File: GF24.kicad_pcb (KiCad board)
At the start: 2 copper layers, 110 x 40 mm, 65 parts, among them J1 3220-10-0300-00, Q1 3904, Q2 DMN3731U-7, Q3 DMN3731U-7, Q4 DMP2004K-7, Q5 DMP2004K-7, Q6 DMP2004K-7, SW1 NRST, SW2 BOOT, SW3 ACTION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

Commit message: going to try and reroute everything
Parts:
- removed BAT1, BAT2: Conn_01x01_Pin, MB-Battery:54
- removed BZ1: CSQG703BP, MB-Buzzer:CSQG703BP
- removed C1, C11, C2: 4.7uF, MB-Generic:C1206_medium
- removed C10, C13, C15, C8, C9: 1uF, MB-Generic:C0805_medium
- removed C12, C14, C4: 0.1uF, MB-Generic:C0603_medium
- removed C3: 10nF, MB-Generic:C0402_medium
- removed C5, C6: 10pF, MB-Generic:C0402_medium
- removed D1: D, MB-SOD:SOD-123-2
- removed D2, D3, D4: LED, MB-Opto:Kingbright-APDA3020
- removed D5: APBDA3020SURKCGKC-GX, MB-Opto:Kingbright-APBDA3020
- removed J1: 3220-10-0300-00, MB-Conn:CONN_3220-10-0100-00_CNC
- removed Q1: 3904, MB-SOT:SOT-23-3
- removed Q2, Q3: DMN3731U-7, MB-SOT:SOT-23-3
- removed Q4, Q5, Q6: DMP2004K-7, MB-SOT:SOT-23-3
- removed R1, R10, R13, R19, R21, R4: 10k, MB-Generic:R0603_medium
- removed R11, R12: 4.7k, MB-Generic:R0603_medium
- removed R14, R17, R18, R20, R22, R23, R3: 1k, MB-Generic:R0603_medium
- removed R15, R16: 47, MB-Generic:R0603_medium
- removed R2: 180, MB-Generic:R0603_medium
- removed R5: 1.5k, MB-Generic:R0603_medium
- removed R6: 4.12k, MB-Generic:R0603_medium
- removed R7, R8: 127, MB-Generic:R0603_medium
- removed R9: 51, MB-Generic:R0603_medium
- removed SW1: NRST, MB-SW:PTS815SJM250SMTRLFS
- removed SW2: BOOT, MB-SW:CJS-1200TA
- removed SW3: ACTION, Connector_Molex:Molex_MicroClasp_55932-0410_1x04_P2.00mm_Vertical
- removed SW4: ON/OFF, MB-SW:1101M2S5AQE2
- removed SW5: MODE, MB-SW:1101M2S5AQE2
- removed TH1: 10K, MB-Generic:R0603_medium
- removed U1: STM32F031C4T6, MB-STM:LQFP-48_7x7mm_P0.5mm
- removed U2: SAM-M10Q, MB-GNSS:SAM-M10Q
- removed U3: TPS745, MB-DFN:6-WDFN
- removed U4: LTC1733, MB-MSOP:10-MSOP
- removed U5: M24256, MB-DFN:8-UFDFN
- removed U6: 2137160001, MB-Conn:MOLEX_2137160001
- removed Y1: CS06465-32M, MB-Crystal:CS06465-32M
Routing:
- net GND: track 71.2 -> 0.00 mm, vias 34 -> 0
- net PG: track 65.5 -> 0.00 mm, vias 1 -> 0
- net N-CHRG: track 55.0 -> 0.00 mm
- net GNSS-TIMEPULSE: track 50.9 -> 0.00 mm
- net NRST: track 45.5 -> 0.00 mm
- net GNSS-N-RESET: track 44.2 -> 0.00 mm
- net MODE: track 41.0 -> 0.00 mm
- net N-FAULT: track 36.2 -> 0.00 mm
- net 3V3: track 35.7 -> 0.00 mm, vias 3 -> 0
- net BUTTON: track 33.9 -> 0.00 mm
- net STM32-TX: track 33.7 -> 0.00 mm
- net STM32-RX: track 33.4 -> 0.00 mm
- net /MODE-H: track 32.0 -> 0.00 mm
- net STATR: track 18.8 -> 0.00 mm, vias 1 -> 0
- net SDA: track 18.3 -> 0.00 mm
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- removed copper zone on F.Cu, net /REG_I
- removed copper zone on F.Cu, net 3V3
- removed copper zone on F.Cu, net BAT+
- removed copper zone on B.Cu, net GND
- removed copper zone on F.Cu, net VBUS
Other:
- board outline removed

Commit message: making things smaller
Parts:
- added C1: 4.7uF, MB-Generic:C1206_medium, F.Cu at (126.6, 62.2)
- added C10: 1uF, MB-Generic:C0805_medium, F.Cu at (168.0, 31.1)
- added C11: 4.7uF, MB-Generic:C1206_medium, F.Cu at (126.6, 68.9)
- added C12: 0.1uF, MB-Generic:C0603_medium, F.Cu at (134.9, 54.8)
- added C13: 1uF, MB-Generic:C0805_medium, F.Cu at (168.0, 34.2)
- added C14: 0.1uF, MB-Generic:C0603_medium, F.Cu at (134.9, 57.4)
- added C15: 1uF, MB-Generic:C0805_medium, F.Cu at (168.0, 37.2)
- added C2: 4.7uF, MB-Generic:C1206_medium, F.Cu at (126.6, 65.5)
- added C3: 10nF, MB-Generic:C0402_medium, F.Cu at (165.5, 67.0)
- added C4: 0.1uF, MB-Generic:C0603_medium, F.Cu at (134.9, 52.2)
- added C5: 10pF, MB-Generic:C0402_medium, F.Cu at (165.5, 69.1)
- added C6: 10pF, MB-Generic:C0402_medium, F.Cu at (165.5, 71.3)
- added C8: 1uF, MB-Generic:C0805_medium, F.Cu at (168.0, 25.1)
- added C9: 1uF, MB-Generic:C0805_medium, F.Cu at (168.0, 28.1)
- added CR1: M24C02-WMN6TP, MB-SOIC:SO-8_STM, F.Cu at (133.8, 63.8)
- added D1: D, MB-SOD:SOD-123-2, F.Cu at (161.3, 53.2)
- added D2: LED, MB-Opto:Kingbright-APDA3020, F.Cu at (146.9, 65.9)
- added D3: LED, MB-Opto:Kingbright-APDA3020, F.Cu at (146.9, 68.4)
- added D4: LED, MB-Opto:Kingbright-APDA3020, F.Cu at (146.9, 70.8)
- added D5: APBDA3020SURKCGKC-GX, MB-Opto:Kingbright-APBDA3020, F.Cu at (153.2, 70.7)
- added J1: Conn_ARM_SWD_TagConnect_TC2030, Connector:Tag-Connect_TC2030-IDC-FP_2x03_P1.27mm_Vertical, F.Cu at (128.5, 55.7)
- added J2: USB4110GFA, MB-Conn:GCT_USB4110GFA, F.Cu at (150.3, 57.8)
- added J3: S2B-PH-SM4-TB, MB-Conn:JST_S2B-PH-SM4-TB, F.Cu at (160.6, 32.1)
- added Q1: 3904, MB-SOT:SOT-23-3, F.Cu at (140.8, 42.8)
- added Q2: DMN3731U-7, MB-SOT:SOT-23-3, F.Cu at (140.8, 47.0)
- added Q3: DMN3731U-7, MB-SOT:SOT-23-3, F.Cu at (140.8, 51.2)
- added Q4: DMP2004K-7, MB-SOT:SOT-23-3, F.Cu at (140.8, 55.5)
- added Q5: DMP2004K-7, MB-SOT:SOT-23-3, F.Cu at (140.8, 59.7)
- added Q6: DMP2004K-7, MB-SOT:SOT-23-3, F.Cu at (140.8, 63.9)
- added R1: 10k, MB-Generic:R0603_medium, F.Cu at (145.2, 41.7)
- added R10: 10k, MB-Generic:R0603_medium, F.Cu at (148.9, 48.8)
- added R11: 4.7k, MB-Generic:R0603_medium, F.Cu at (148.9, 51.2)
- added R12: 4.7k, MB-Generic:R0603_medium, F.Cu at (148.9, 53.5)
- added R13: 10k, MB-Generic:R0603_medium, F.Cu at (152.6, 41.7)
- added R14: 1k, MB-Generic:R0603_medium, F.Cu at (152.6, 44.0)
- added R15: 47, MB-Generic:R0603_medium, F.Cu at (152.6, 46.4)
- added R16: 47, MB-Generic:R0603_medium, F.Cu at (152.6, 48.8)
- added R17: 1k, MB-Generic:R0603_medium, F.Cu at (152.6, 51.2)
- added R18: 1k, MB-Generic:R0603_medium, F.Cu at (152.6, 53.5)
- added R19: 10k, MB-Generic:R0603_medium, F.Cu at (156.3, 41.7)
- added R2: 180, MB-Generic:R0603_medium, F.Cu at (145.2, 44.0)
- added R20: 1k, MB-Generic:R0603_medium, F.Cu at (156.3, 44.0)
- added R21: 10k, MB-Generic:R0603_medium, F.Cu at (156.3, 46.4)
- added R22: 1k, MB-Generic:R0603_medium, F.Cu at (156.3, 48.8)
- added R23: 1k, MB-Generic:R0603_medium, F.Cu at (156.3, 51.2)
- added R3: 1k, MB-Generic:R0603_medium, F.Cu at (145.2, 46.4)
- added R4: 10k, MB-Generic:R0603_medium, F.Cu at (145.2, 48.8)
- added R5: 1.5k, MB-Generic:R0603_medium, F.Cu at (145.2, 51.2)
- added R6: 4.12k, MB-Generic:R0603_medium, F.Cu at (145.2, 53.5)
- added R7: 127, MB-Generic:R0603_medium, F.Cu at (148.9, 41.7)
- added R8: 127, MB-Generic:R0603_medium, F.Cu at (148.9, 44.0)
- added R9: 51, MB-Generic:R0603_medium, F.Cu at (148.9, 46.4)
- added SW1: ~, MB-SW:PTS815SJM250SMTRLFS, F.Cu at (160.7, 68.0)
- added SW2: BOOT, MB-SW:CJS-1200TA, F.Cu at (158.5, 37.5)
- added SW3: ~, MB-SW:TL1016AAF160QG, F.Cu at (153.6, 67.5)
- added SW4: ~, MB-SW:SW_500ASSP1SM6QE, F.Cu at (131.0, 30.5)
- added SW5: ~, MB-SW:SW_500ASSP1SM6QE, F.Cu at (131.0, 44.2)
- added TH1: 10K, MB-Generic:R0603_medium, F.Cu at (156.3, 53.5)
- added U1: STM32F031C4T6, MB-STM:LQFP-48_7x7mm_P0.5mm, F.Cu at (163.8, 46.2)
- added U2: SAM-M10Q, MB-GNSS:SAM-M10Q, F.Cu at (147.1, 32.0)
- added U3: TPS745, MB-DFN:6-WDFN, F.Cu at (169.3, 70.6)
- added U4: LTC1733, MB-MSOP:10-MSOP-TE, F.Cu at (133.0, 69.4)
- added U5: ST-025BH, MB-Buzzer:ST-025BH_SOB, F.Cu at (163.5, 60.4)
- added Y1: CS06465-32M, MB-Crystal:CS06465-32M, F.Cu at (169.2, 67.5)
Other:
- board outline added: 90 x 40 mm

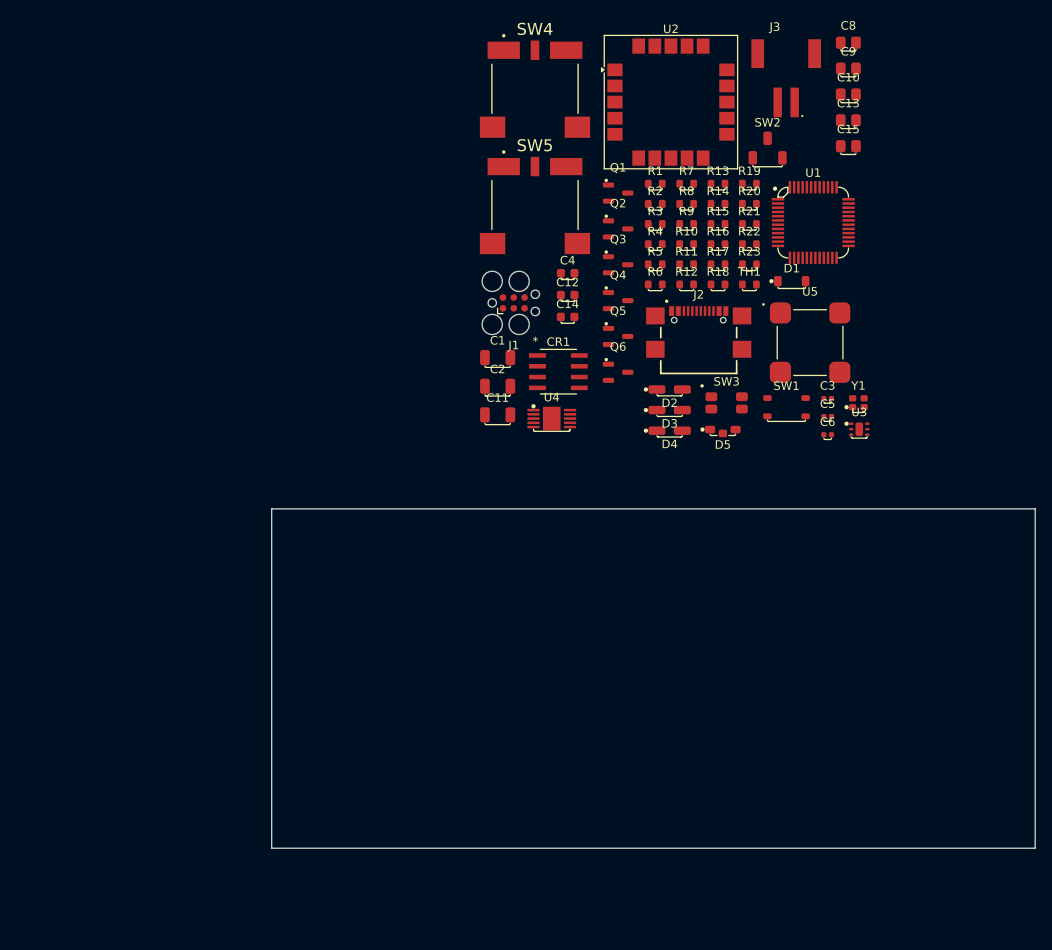
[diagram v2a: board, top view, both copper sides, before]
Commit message: added mouse bites. need to do stackup
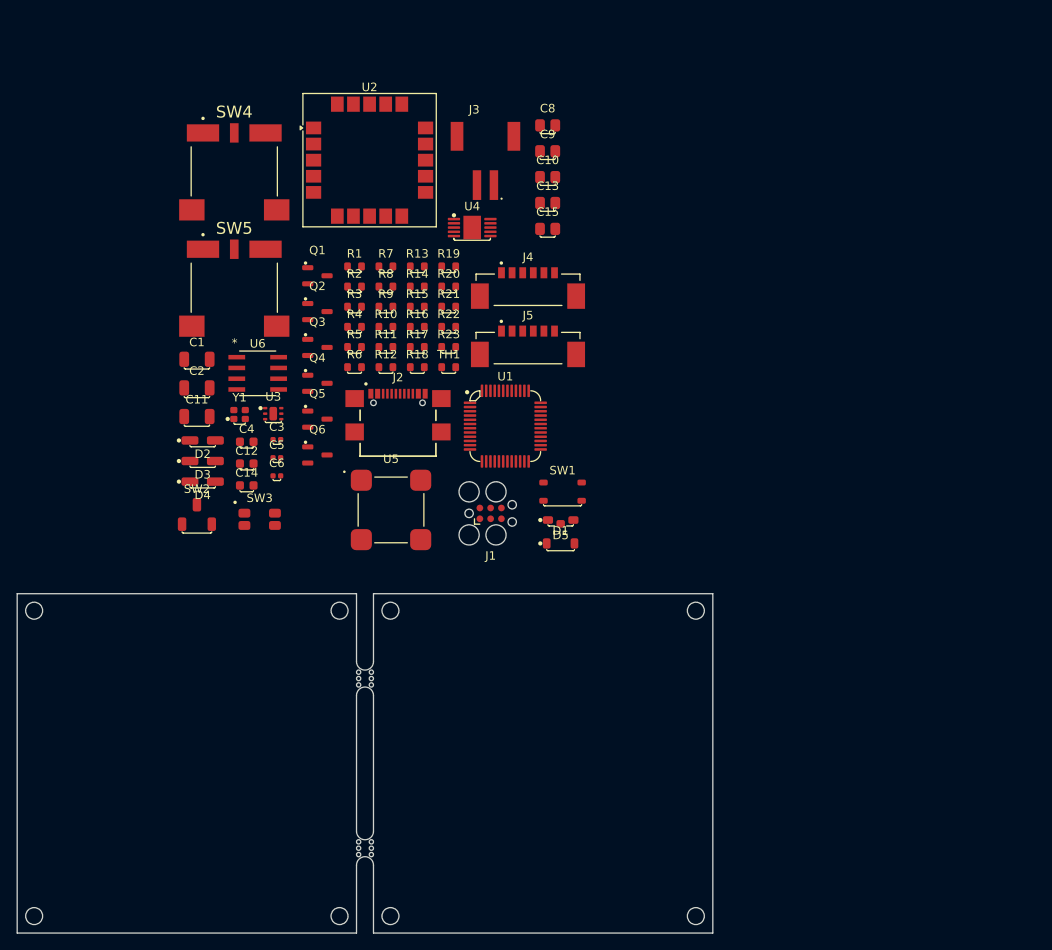
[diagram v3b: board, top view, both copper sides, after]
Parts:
- removed CR1: M24C02-WMN6TP, MB-SOIC:SO-8_STM
- added J4: 0533980671, MB-Conn:MOLEX_0533980671, F.Cu at (130.2, 52.8)
- added J5: 0533980671, MB-Conn:MOLEX_0533980671, F.Cu at (130.2, 59.7)
- added U6: M24C02-WMN6TP, MB-SOIC:SO-8_STM, F.Cu at (98.3, 64.0)
- added mouse-bite-2mm-slot: VAL**, MB-Tab:mouse-bite-2mm-slot, F.Cu at (111.0, 100.0)
- added mouse-bite-2mm-slot: VAL**, MB-Tab:mouse-bite-2mm-slot, F.Cu at (111.0, 120.0)
- J1: footprint Connector:Tag-Connect_TC2030-IDC-FP_2x03_P1.27mm_Vertical -> MB-Conn:Tag-Connect_TC2030-IDC-FP_2x03_P1.27mm_Vertical
- moved SW2 79.9 mm to (91.2, 80.7)
- moved Y1 73.0 mm to (96.2, 68.9)
- moved U3 69.1 mm to (100.2, 68.8)
- moved C3 65.1 mm to (100.6, 71.8)
- moved C5 65.1 mm to (100.6, 74.0)
- moved C6 65.1 mm to (100.6, 76.1)
- moved SW3 56.7 mm to (98.6, 81.2)
- moved D2 55.4 mm to (91.9, 71.9)
- moved D3 55.4 mm to (91.9, 74.4)
- moved D4 55.4 mm to (91.9, 76.8)
- moved U5 53.2 mm to (114.1, 80.1)
- moved U1 43.5 mm to (127.5, 70.2)
- moved C12 42.7 mm to (97.1, 74.7)
- moved C14 42.7 mm to (97.1, 77.2)
- moved C4 42.7 mm to (97.1, 72.1)
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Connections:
- U1 pad 11: GNSS-N-RESET -> /GNSS-ST-N-RESET
- U1 pad 12: GNSS-RX -> /GNSS-ST-RX
- U1 pad 13: GNSS-TX -> /GNSS-ST-TX
- U1 pad 14: GNSS-TIMEPULSE -> /GNSS-ST-TIMEPULSE
- U1 pad 42: unconnected-(U1-PB6-Pad42) -> BUZZER
- U2 pad 1: GND -> GNSS-GND
- U2 pad 10: GND -> GNSS-GND
- U2 pad 11: GND -> GNSS-GND
- U2 pad 15: GND -> GNSS-GND
- U2 pad 16: GND -> GNSS-GND
- U2 pad 17: +3V3 -> GNSS-3V3
- U2 pad 2: +3V3 -> GNSS-3V3
- U2 pad 20: GND -> GNSS-GND
- U2 pad 4: GND -> GNSS-GND
- U2 pad 5: GND -> GNSS-GND
- U2 pad 6: GND -> GNSS-GND
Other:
- board size 90 x 40 mm -> 82 x 40 mm

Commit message: board setup mostly complete. need to do net classes properly
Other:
- copper layers 2 -> 4
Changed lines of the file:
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@@
 	(generator_version "8.0")
 	(general
-		(thickness 1.6)
+		(thickness 1.547)
 		(legacy_teardrops no)
 	)
@@
 	(layers
 		(0 "F.Cu" signal)
+		(1 "In1.Cu" signal)
+		(2 "In2.Cu" signal)
 		(31 "B.Cu" signal)
 		(32 "B.Adhes" user "B.Adhesive")
@@
 			(layer "F.Cu"
 				(type "copper")
+				(thickness 0.0175)
+			)
+			(layer "dielectric 1"
+				(type "prepreg")
+				(thickness 0.196)
+				(material "7628")
+				(epsilon_r 4.74)
+				(loss_tangent 0.02)
+			)
+			(layer "In1.Cu"
+				(type "copper")
 				(thickness 0.035)
 			)
-			(layer "dielectric 1"
+			(layer "dielectric 2"
 				(type "core")
-				(thickness 1.51)
-				(material "FR4")
-				(epsilon_r 4.5)
+				(thickness 1.03)
+				(material "Core")
+				(epsilon_r 4.6)
+				(loss_tangent 0.02)
+			)
+			(layer "In2.Cu"
+				(type "copper")
+				(thickness 0.035)
+			)
+			(layer "dielectric 3"
+				(type "prepreg")
+				(thickness 0.196)
+				(material "7628")
+				(epsilon_r 4.74)
 				(loss_tangent 0.02)
 			)
 			(layer "B.Cu"
 				(type "copper")
-				(thickness 0.035)
+				(thickness 0.0175)
 			)
 			(layer "B.Mask"

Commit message: initial layout
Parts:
- C11, C12, C13, C15, D1, J1, J2, J3, J5, Q1, R13, R14, R2, R5, R6, SW4, SW5, TH1, U4, U5: moved to B.Cu
- moved Q1 79.5 mm to (130.2, 128.0), turned to 180 degrees
- moved J5 75.4 mm to (74.0, 110.0), turned to 90 degrees
- moved J4 75.3 mm to (124.0, 127.8), turned to 180 degrees
- moved U2 74.3 mm to (90.0, 110.0)
- moved U6 73.0 mm to (137.0, 126.0), turned to 90 degrees
- moved R2 73.0 mm to (130.5, 123.8), turned to 90 degrees
- moved C2 69.6 mm to (136.0, 119.0), turned to -135 degrees
- moved J3 69.5 mm to (120.0, 111.1), turned to -90 degrees
- moved C9 67.6 mm to (137.5, 105.2)
- moved C8 67.5 mm to (135.2, 102.2), turned to -90 degrees
- moved R11 65.1 mm to (138.0, 121.2)
- moved C13 62.6 mm to (124.5, 106.0), turned to -90 degrees
- moved SW4 62.2 mm to (123.0, 96.0)
- moved C15 62.0 mm to (138.2, 108.8)
- moved R12 62.0 mm to (139.0, 119.8)
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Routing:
- added copper zone on B.Cu, net GND
- added copper zone on F.Cu, net GND

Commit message: another round of layout
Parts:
- removed mouse-bite-2mm-slot (x2): VAL**, MB-Tab:mouse-bite-2mm-slot
- moved TH1 8.70 mm to (133.0, 110.2), turned to -90 degrees
- moved C12 2.80 mm to (135.8, 107.8)
- moved R7 2.49 mm to (141.5, 94.8), turned to 90 degrees
- moved R6 1.95 mm to (127.0, 108.0), turned to 180 degrees
- moved C11 1.35 mm to (133.8, 106.0)
- moved C15 1.27 mm to (139.5, 108.5)
- moved SW4 0.50 mm to (123.0, 96.5)
- moved SW5 0.50 mm to (141.0, 96.5)
- moved C2 0.32 mm to (136.2, 118.8)
- moved R3 0.15 mm to (150.3, 102.2)
- moved R4 0.15 mm to (147.3, 102.2)
- moved SW3 0.15 mm to (150.3, 98.2)
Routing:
- net GND: track 0.00 -> 74.9 mm, vias 0 -> 18
- net NRST: track 0.00 -> 48.6 mm, vias 0 -> 3
- net GNSS-GND: track 0.00 -> 34.2 mm, vias 0 -> 62
- net GNSS-TX: track 0.00 -> 25.5 mm, vias 0 -> 2
- net GNSS-RX: track 0.00 -> 25.4 mm, vias 0 -> 2
- net /SWDCLK: track 0.00 -> 22.4 mm, vias 0 -> 2
- net N-CHRG: track 0.00 -> 22.2 mm, vias 0 -> 2
- net STATR: track 0.00 -> 22.0 mm, vias 0 -> 2
- net BUTTON: track 0.00 -> 21.3 mm, vias 0 -> 2
- net +3V3: track 0.00 -> 21.1 mm, vias 0 -> 3
- net GNSS-N-RESET: track 0.00 -> 20.9 mm, vias 0 -> 2
- net /SWDIO: track 0.00 -> 20.7 mm, vias 0 -> 2
- net VBUS: track 0.00 -> 19.4 mm, vias 0 -> 4
- net GNSS-TIMEPULSE: track 0.00 -> 18.0 mm, vias 0 -> 2
- net MODE: track 0.00 -> 16.6 mm, vias 0 -> 3
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- added copper zone on F.Cu, net +3V3
- added copper zone on In2.Cu, net /REG_I
- added copper zone on B.Cu, net BAT+
- added copper zone on In1.Cu, net GNSS-3V3
- added copper zone on B.Cu, net GNSS-GND
- added copper zone on F.Cu, net GNSS-GND
- added copper zone on B.Cu, net VBUS
- removed copper zone on F.Cu, net GND

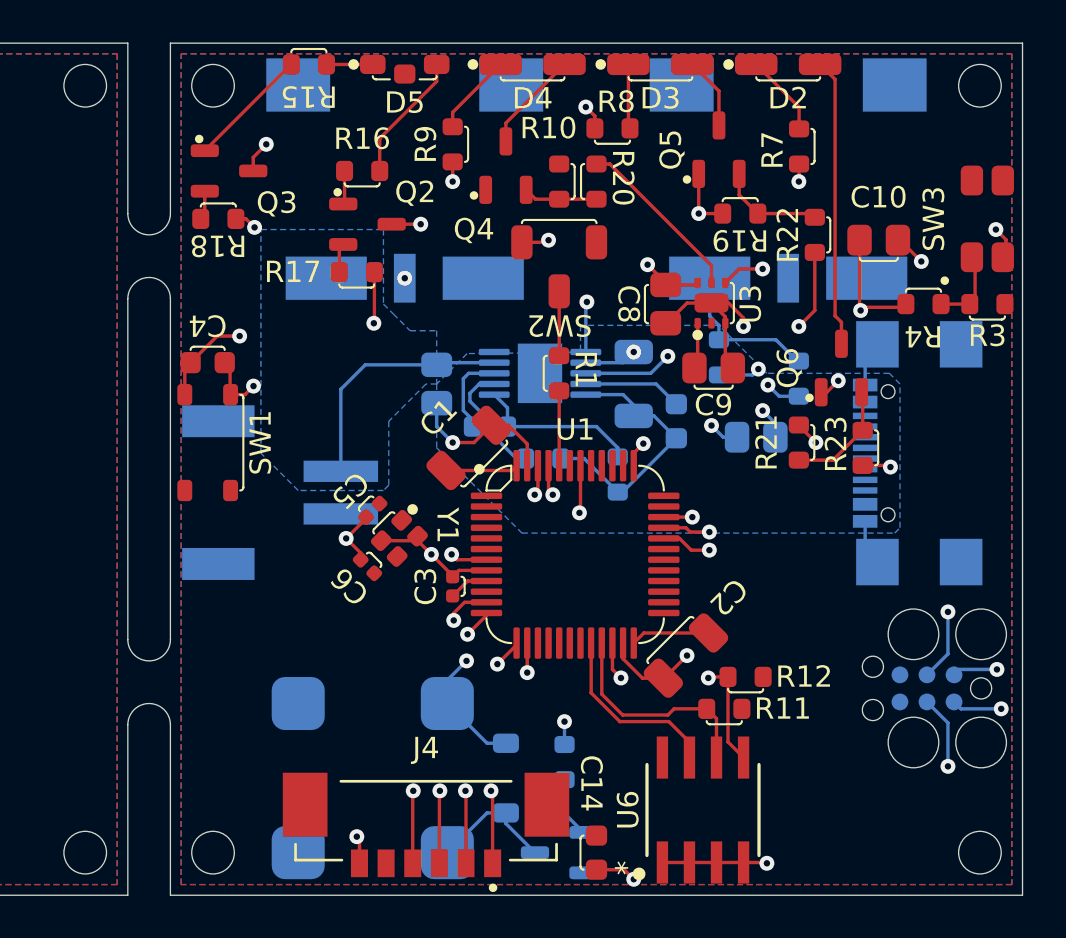
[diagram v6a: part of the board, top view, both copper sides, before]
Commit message: still need to add test points, BOM
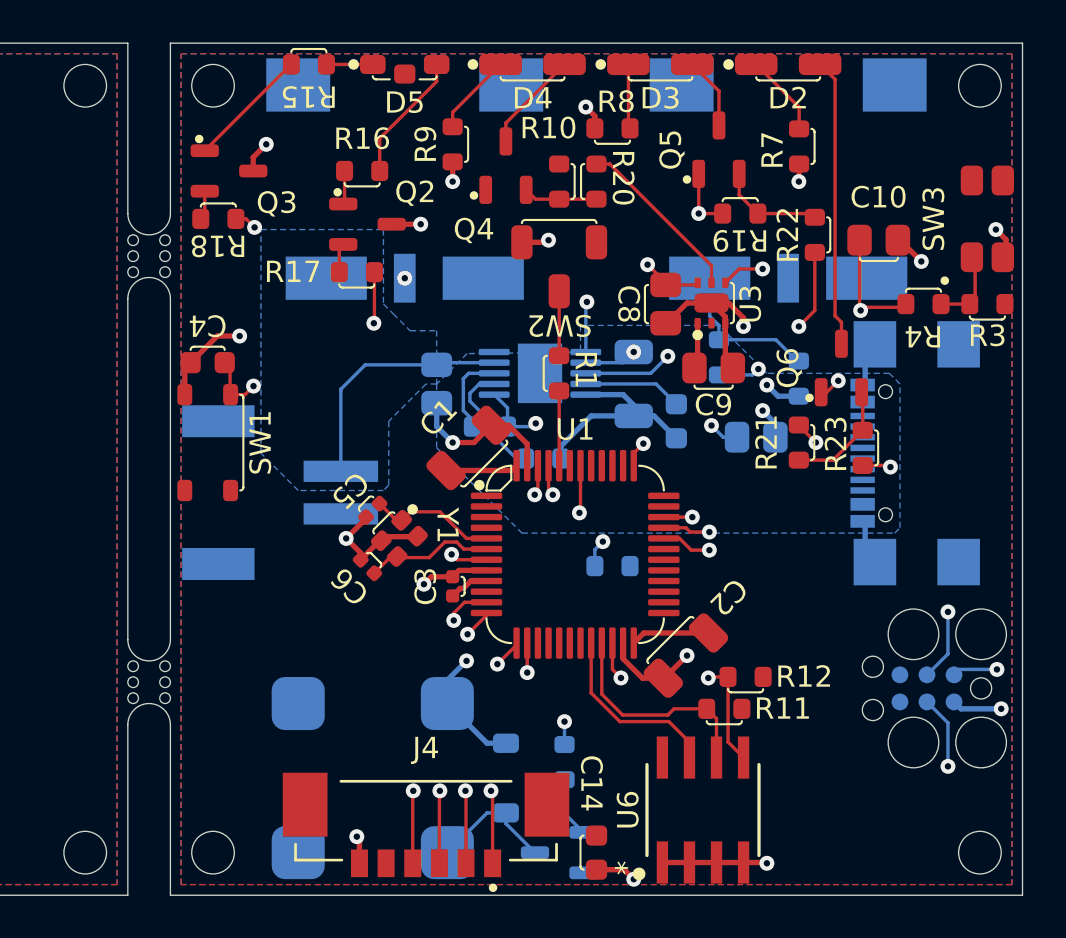
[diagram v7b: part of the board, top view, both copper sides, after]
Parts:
- added mouse-bite-2mm-slot: VAL**, MB-Tab:mouse-bite-2mm-slot, F.Cu at (111.0, 120.0)
- added mouse-bite-2mm-slot: VAL**, MB-Tab:mouse-bite-2mm-slot, F.Cu at (111.0, 100.0)
- moved TH1 4.31 mm to (132.8, 114.5), turned to 0 degrees
- moved J2 0.12 mm to (145.6, 109.2)
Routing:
- net /OSC-OUT: track 0.00 -> 6.06 mm
- net /OSC-IN: track 0.00 -> 6.03 mm
- net /CH-TH-DIV: track 7.77 -> 11.3 mm, vias 0 -> 2
- net GND: track 74.9 -> 72.7 mm

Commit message: added some final touches
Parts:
- added G***: LOGO, MB-Initials:initials-5mm, B.Cu at (139.4, 125.0)
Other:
- board text added: "+"
- board text added: "-"
- board text added: "ACTION"
- board text added: "BAT+"
- board text added: "BOOT"
- board text added: "BUT"
- board text added: "BUZZ"
- board text added: "GeoFence Rev. 1"
- board text added: "MOD"
- board text added: "MODE"
- board text added: "NR"
- board text added: "NRST"
- board text added: "PLEDS"
- board text added: "PWR"
- board text added: "RESET"
- board text added: "SCL"
- board text added: "SDA"
- board text added: "STRX"
- board text added: "STTX"
- board text added: "SWCK"
- board text added: "SWIO"
- board text added: "TC"
- board text added: "TP"
- board text added: "VBUS"
